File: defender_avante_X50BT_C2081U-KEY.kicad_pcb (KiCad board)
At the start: 2 copper layers, 172.7 x 61 mm, 85 parts, among them CN301 CONNECTOR_M_006_20_SPECIAL, J300 JUMPER, J301 JUMPER, J302 JUMPER, J303 JUMPER, J304 JUMPER, J305 JUMPER, J306 JUMPER, J307 JUMPER, J308 JUMPER, J309 JUMPER, J310 JUMPER, J311 JUMPER, J312 JUMPER, J313 JUMPER, J314 JUMPER, J315 JUMPER, J316 JUMPER, J317 JUMPER, J318 JUMPER, J319 JUMPER, J320 JUMPER, J321 JUMPER, J322 JUMPER, J323 JUMPER, J324 JUMPER, J325 JUMPER, J326 JUMPER, J327 JUMPER, J328 JUMPER, J329 JUMPER, J330 JUMPER, J331 JUMPER, J332 JUMPER, J333 JUMPER, J334 JUMPER, J335 JUMPER, J336 JUMPER, J337 JUMPER, Q300 BJT_NPN_GENERAL, U300 TM1668

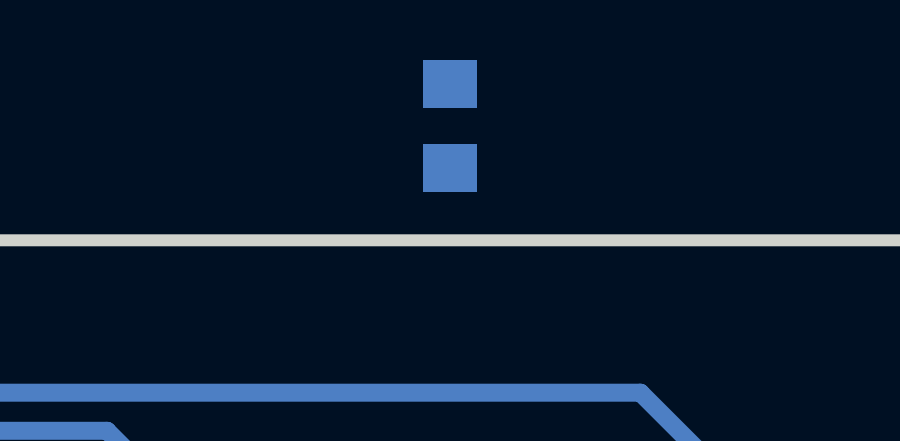
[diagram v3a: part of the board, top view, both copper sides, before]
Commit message: Удалена лишняя перемычка J314
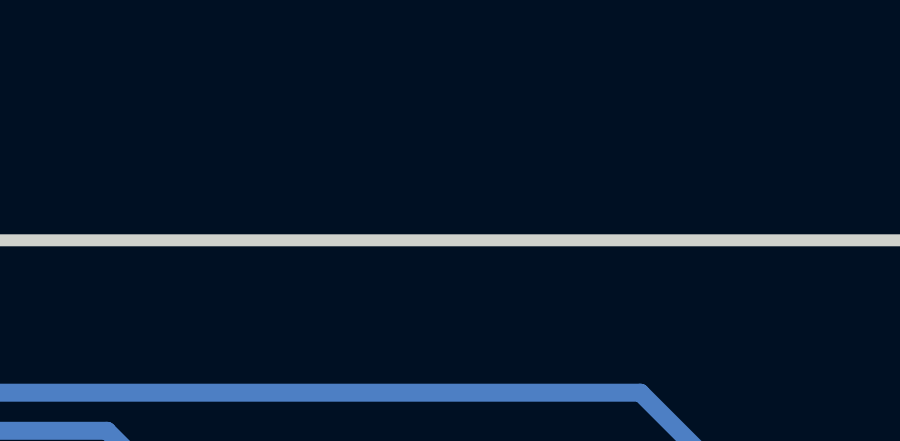
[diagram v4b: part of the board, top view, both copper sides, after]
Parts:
- removed the J314 at (118.1, 71.1)
- renumbered J315 to J314, J316 to J315, J317 to J316, J318 to J317, J319 to J318, J320 to J319, J321 to J320, J322 to J321, J323 to J322, J324 to J323, J325 to J324, J326 to J325, J327 to J326, J328 to J327, J329 to J328, J330 to J329, J331 to J330, J332 to J331, J333 to J332, J334 to J333, J335 to J334, J336 to J335, J337 to J336
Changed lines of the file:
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@@
     (tracks 502)
     (zones 0)
-    (modules 85)
+    (modules 84)
     (nets 49)
   )
@@
   (title_block
     (title defender_avante_X50BT_C2081U-KEY)
-    (date 2019-05-23)
+    (date 2019-06-04)
     (rev 2)
     (company "Igor Vladimirovich Ivanov")
@@
     (at 77.47 111.76 180)
     (attr smd)
-    (fp_text reference J332 (at 0 1.905 180) (layer B.SilkS)
+    (fp_text reference J331 (at 0 1.905 180) (layer B.SilkS)
       (effects (font (size 1 1) (thickness 0.2)) (justify mirror))
     )
@@
     (at 74.93 87.63 90)
     (attr smd)
-    (fp_text reference J334 (at 0 -1.905 270) (layer B.SilkS)
+    (fp_text reference J333 (at 0 -1.905 270) (layer B.SilkS)
       (effects (font (size 1 1) (thickness 0.2)) (justify mirror))
     )
@@
     (at 82.55 103.505 180)
     (attr smd)
-    (fp_text reference J329 (at 0 1.905 180) (layer B.SilkS)
+    (fp_text reference J328 (at 0 1.905 180) (layer B.SilkS)
       (effects (font (size 1 1) (thickness 0.2)) (justify mirror))
     )
@@
     (at 95.25 95.25 90)
     (attr smd)
-    (fp_text reference J322 (at 0 -1.905 270) (layer B.SilkS)
+    (fp_text reference J321 (at 0 -1.905 270) (layer B.SilkS)
       (effects (font (size 1 1) (thickness 0.2)) (justify mirror))
     )
@@
     (at 86.36 115.57 180)
     (attr smd)
-    (fp_text reference J326 (at 0 1.905 180) (layer B.SilkS)
+    (fp_text reference J325 (at 0 1.905 180) (layer B.SilkS)
       (effects (font (size 1 1) (thickness 0.2)) (justify mirror))
     )
@@
     (at 107.95 83.82 180)
     (attr smd)
-    (fp_text reference J315 (at 0 1.905 180) (layer B.SilkS)
+    (fp_text reference J314 (at 0 1.905 180) (layer B.SilkS)
       (effects (font (size 1 1) (thickness 0.2)) (justify mirror))
     )
@@
   )
   (module KCL:J-SMD-1206 (layer B.Cu)
-    (at 118.11 71.12 90)
-    (attr smd)
-    (fp_text reference J314 (at 0 -1.905 270) (layer B.SilkS)
-      (effects (font (size 1 1) (thickness 0.2)) (justify mirror))
-    )
-    (fp_text value JUMPER (at 1.905 4.445 180) (layer B.Fab) hide
-      (effects (font (size 1 1) (thickness 0.2)) (justify mirror))
-    )
-    (fp_line (start -1.6 0.8) (end -1.6 -0.8) (layer B.Fab) (width 0.2))
-    (fp_line (start -1.6 -0.8) (end 1.6 -0.8) (layer B.Fab) (width 0.2))
-    (fp_line (start 1.6 0.8) (end 1.6 -0.8) (layer B.Fab) (width 0.2))
-    (fp_line (start -1.6 0.8) (end 1.6 0.8) (layer B.Fab) (width 0.2))
-    (fp_line (start -2.413 1.016) (end -2.413 -1.016) (layer B.SilkS) (width 0.2))
-    (fp_line (start 2.413 1.016) (end 2.413 -1.016) (layer B.SilkS) (width 0.2))
-    (fp_line (start -2.413 1.016) (end 2.413 1.016) (layer B.SilkS) (width 0.2))
-    (fp_line (start -2.413 -1.016) (end 2.413 -1.016) (layer B.SilkS) (width 0.2))
-    (fp_line (start -0.381 0) (end 0.381 0) (layer B.SilkS) (width 0.2))
-    (fp_line (start -2.413 -1.016) (end -2.413 1.016) (layer B.CrtYd) (width 0.1))
-    (fp_line (start 2.413 -1.016) (end -2.413 -1.016) (layer B.CrtYd) (width 0.1))
-    (fp_line (start 2.413 1.016) (end 2.413 -1.016) (layer B.CrtYd) (width 0.1))
-    (fp_line (start -2.413 1.016) (end 2.413 1.016) (layer B.CrtYd) (width 0.1))
-    (pad J smd rect (at 1.4 0 90) (size 1.6 1.8) (layers B.Cu B.Mask)
-      (net 16 /B))
-    (pad J smd rect (at -1.4 0 90) (size 1.6 1.8) (layers B.Cu B.Mask)
-      (net 16 /B))
-  )
-  (module KCL:J-SMD-1206 (layer B.Cu)
     (at 156.21 106.68 90)
     (attr smd)
@@
     (at 69.85 101.6 90)
     (attr smd)
-    (fp_text reference J336 (at 0 1.905 270) (layer B.SilkS)
+    (fp_text reference J335 (at 0 1.905 270) (layer B.SilkS)
       (effects (font (size 1 1) (thickness 0.2)) (justify mirror))
     )
@@
     (at 97.79 115.57 180)
     (attr smd)
-    (fp_text reference J321 (at 4.445 0 180) (layer B.SilkS)
+    (fp_text reference J320 (at 4.445 0 180) (layer B.SilkS)
       (effects (font (size 1 1) (thickness 0.2)) (justify mirror))
     )
@@
     (at 100.33 87.63 90)
     (attr smd)
-    (fp_text reference J319 (at 0 -1.905 270) (layer B.SilkS)
+    (fp_text reference J318 (at 0 -1.905 270) (layer B.SilkS)
       (effects (font (size 1 1) (thickness 0.2)) (justify mirror))
     )
@@
   (module KCL:J-SMD-1206 (layer B.Cu)
     (at 107.95 103.505 180)
-    (fp_text reference J317 (at 0 1.905 180) (layer B.SilkS)
+    (fp_text reference J316 (at 0 1.905 180) (layer B.SilkS)
       (effects (font (size 1 1) (thickness 0.2)) (justify mirror))
     )
@@
     (at 87.63 87.63 90)
     (attr smd)
-    (fp_text reference J324 (at 0 -1.905 270) (layer B.SilkS)
+    (fp_text reference J323 (at 0 -1.905 270) (layer B.SilkS)
       (effects (font (size 1 1) (thickness 0.2)) (justify mirror))
     )
@@
     (at 86.36 111.76 180)
     (attr smd)
-    (fp_text reference J325 (at 0 1.905 180) (layer B.SilkS)
+    (fp_text reference J324 (at 0 1.905 180) (layer B.SilkS)
       (effects (font (size 1 1) (thickness 0.2)) (justify mirror))
     )
@@
     (at 105.41 113.03 180)
     (attr smd)
-    (fp_text reference J318 (at 0 1.905 180) (layer B.SilkS)
+    (fp_text reference J317 (at 0 1.905 180) (layer B.SilkS)
       (effects (font (size 1 1) (thickness 0.2)) (justify mirror))
     )
@@
     (at 69.85 96.52 90)
     (attr smd)
-    (fp_text reference J335 (at 0 1.905 270) (layer B.SilkS)
+    (fp_text reference J334 (at 0 1.905 270) (layer B.SilkS)
       (effects (font (size 1 1) (thickness 0.2)) (justify mirror))
     )
@@
     (at 67.31 96.52 90)
     (attr smd)
-    (fp_text reference J337 (at 0 -1.905 270) (layer B.SilkS)
+    (fp_text reference J336 (at 0 -1.905 270) (layer B.SilkS)
       (effects (font (size 1 1) (thickness 0.2)) (justify mirror))
     )
@@
     (at 107.95 87.63 90)
     (attr smd)
-    (fp_text reference J316 (at 0 -1.905 270) (layer B.SilkS)
+    (fp_text reference J315 (at 0 -1.905 270) (layer B.SilkS)
       (effects (font (size 1 1) (thickness 0.2)) (justify mirror))
     )
@@
     (at 77.47 115.57 180)
     (attr smd)
-    (fp_text reference J333 (at 0 1.905 180) (layer B.SilkS)
+    (fp_text reference J332 (at 0 1.905 180) (layer B.SilkS)
       (effects (font (size 1 1) (thickness 0.2)) (justify mirror))
     )
@@
     (at 82.55 83.82 180)
     (attr smd)
-    (fp_text reference J327 (at 0 1.905 180) (layer B.SilkS)
+    (fp_text reference J326 (at 0 1.905 180) (layer B.SilkS)
       (effects (font (size 1 1) (thickness 0.2)) (justify mirror))
     )
@@
     (at 77.47 95.25 180)
     (attr smd)
-    (fp_text reference J331 (at 0 1.905 180) (layer B.SilkS)
+    (fp_text reference J330 (at 0 1.905 180) (layer B.SilkS)
       (effects (font (size 1 1) (thickness 0.2)) (justify mirror))
     )
@@
     (at 91.44 111.76 180)
     (attr smd)
-    (fp_text reference J323 (at 0 1.905 180) (layer B.SilkS)
+    (fp_text reference J322 (at 0 1.905 180) (layer B.SilkS)
       (effects (font (size 1 1) (thickness 0.2)) (justify mirror))
     )
@@
     (at 97.79 113.03 180)
     (attr smd)
-    (fp_text reference J320 (at 0 1.905 180) (layer B.SilkS)
+    (fp_text reference J319 (at 0 1.905 180) (layer B.SilkS)
       (effects (font (size 1 1) (thickness 0.2)) (justify mirror))
     )
@@
     (at 81.28 111.76 90)
     (attr smd)
-    (fp_text reference J330 (at -4.445 0 270) (layer B.SilkS)
+    (fp_text reference J329 (at -4.445 0 270) (layer B.SilkS)
       (effects (font (size 1 1) (thickness 0.2)) (justify mirror))
     )
@@
     (at 82.55 87.63 90)
     (attr smd)
-    (fp_text reference J328 (at 0 -1.905 270) (layer B.SilkS)
-      (effects (font (size 1 1) (thickness 0.2)) (justify mirror))
-    )
+    (fp_text reference J327 (at 0 -1.905 270) (layer B.SilkS)
+      (effects (font (size 1 1) (thickness 0.2)) (justify mirror))
+    )

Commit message: Схема и плата оформлены корректно
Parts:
- added VLS300: VIRTUAL_LED-SPACER, KCL:VLS-BR, F.Cu at (229.9, 85.1)
- added VLS301: VIRTUAL_LED-SPACER, KCL:VLS-BR, F.Cu at (214.6, 105.4)
- W300: value ENCODER_CONTACTING_INC_B -> ENCODER_CONTACTING_INC_B_C
- moved R324 5.68 mm to (118.1, 85.1)
- moved R325 5.68 mm to (113.0, 87.6)
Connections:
- R324 pad 2: /A -> /B
- R325 pad 2: /B -> /A
- U300 pad 13: Net-(R325-Pad1) -> Net-(R324-Pad1)
- U300 pad 14: Net-(R324-Pad1) -> Net-(R325-Pad1)
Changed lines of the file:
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@@
   (general
     (thickness 1.5)
-    (drawings 27)
+    (drawings 21)
     (tracks 502)
     (zones 0)
-    (modules 84)
+    (modules 86)
     (nets 49)
   )
@@
     (add_net V)
   )
+  (module KCL:VLS-BR locked (layer F.Cu)
+    (at 214.63 105.41)
+    (attr virtual)
+    (fp_text reference VLS301 (at 0 7.62) (layer F.SilkS)
+      (effects (font (size 1 1) (thickness 0.2)))
+    )
+    (fp_text value VIRTUAL_LED-SPACER (at 28.575 1.27) (layer F.Fab) hide
+      (effects (font (size 1 1) (thickness 0.2)))
+    )
+    (fp_circle (center 0 0) (end 2.6 0) (layer F.CrtYd) (width 0.1))
+    (fp_circle (center 0 0) (end 2.6 0) (layer F.SilkS) (width 0.2))
+    (fp_circle (center 0 0) (end 2.6 0) (layer F.Fab) (width 0.2))
+  )
+  (module KCL:VLS-BR locked (layer F.Cu)
+    (at 229.87 85.09)
+    (attr virtual)
+    (fp_text reference VLS300 (at 0 -3.81) (layer F.SilkS)
+      (effects (font (size 1 1) (thickness 0.2)))
+    )
+    (fp_text value VIRTUAL_LED-SPACER (at 13.335 1.27) (layer F.Fab) hide
+      (effects (font (size 1 1) (thickness 0.2)))
+    )
+    (fp_circle (center 0 0) (end 2.6 0) (layer F.Fab) (width 0.2))
+    (fp_circle (center 0 0) (end 2.6 0) (layer F.SilkS) (width 0.2))
+    (fp_circle (center 0 0) (end 2.6 0) (layer F.CrtYd) (width 0.1))
+  )
   (module KCL:R-MFR-12 (layer F.Cu)
     (at 129.54 109.22)
@@
   )
   (module KCL:R-MFR-12 (layer F.Cu)
-    (at 113.03 87.63 180)
-    (fp_text reference R324 (at -6.35 0 180) (layer F.SilkS)
+    (at 118.11 85.09 180)
+    (fp_text reference R324 (at 0 2.54 180) (layer F.SilkS)
       (effects (font (size 1 1) (thickness 0.2)))
     )
-    (fp_text value RESISTOR_GENERAL (at -16.51 0 180) (layer F.Fab) hide
+    (fp_text value RESISTOR_GENERAL (at -11.43 0 180) (layer F.Fab) hide
       (effects (font (size 1 1) (thickness 0.2)))
     )
@@
     (fp_line (start 0.635 0.635) (end 1.27 0) (layer F.SilkS) (width 0.2))
     (pad 2 thru_hole rect (at 2.54 0 180) (size 2 2) (drill 0.5) (layers B.Cu B.Mask)
-      (net 17 /A))
+      (net 16 /B))
     (pad 1 thru_hole rect (at -2.54 0 180) (size 2 2) (drill 0.5) (layers B.Cu B.Mask)
       (net 42 "Net-(R324-Pad1)"))
   )
   (module KCL:R-MFR-12 (layer F.Cu)
-    (at 118.11 85.09 180)
-    (fp_text reference R325 (at 0 2.54 180) (layer F.SilkS)
+    (at 113.03 87.63 180)
+    (fp_text reference R325 (at -6.35 0 180) (layer F.SilkS)
       (effects (font (size 1 1) (thickness 0.2)))
     )
-    (fp_text value RESISTOR_GENERAL (at -11.43 0 180) (layer F.Fab) hide
+    (fp_text value RESISTOR_GENERAL (at -16.51 0 180) (layer F.Fab) hide
       (effects (font (size 1 1) (thickness 0.2)))
     )
@@
       (net 41 "Net-(R325-Pad1)"))
     (pad 2 thru_hole rect (at 2.54 0 180) (size 2 2) (drill 0.5) (layers B.Cu B.Mask)
-      (net 16 /B))
+      (net 17 /A))
   )
   (module KCL:R-MFR-12 (layer F.Cu)
@@
       (net 32 "Net-(U300-Pad15)"))
     (pad 14 smd rect (at 4.6 -5.715 180) (size 2.2 0.6) (layers B.Cu B.Mask)
-      (net 42 "Net-(R324-Pad1)"))
+      (net 41 "Net-(R325-Pad1)"))
     (pad 19 smd rect (at 4.6 0.635 180) (size 2.2 0.6) (layers B.Cu B.Mask)
       (net 31 "Net-(U300-Pad19)"))
@@
       (net 30 "Net-(U300-Pad16)"))
     (pad 13 smd rect (at 4.6 -6.985 180) (size 2.2 0.6) (layers B.Cu B.Mask)
-      (net 41 "Net-(R325-Pad1)"))
+      (net 42 "Net-(R324-Pad1)"))
     (pad 12 smd rect (at -4.6 -6.985 180) (size 2.2 0.6) (layers B.Cu B.Mask)
       (net 48 "Net-(R323-Pad2)"))
@@
   (module KCL:LED-ROUND-03.0-UNI-SH-SPACER locked (layer F.Cu)
     (at 229.87 85.09 45)
-    (fp_text reference LED300 (at 4.041115 -4.041115 180) (layer F.SilkS)
+    (fp_text reference LED300 (at 5.388154 -5.388154 180) (layer F.SilkS)
       (effects (font (size 1 1) (thickness 0.2)))
     )
@@
       (effects (font (size 1 1) (thickness 0.2)))
     )
-    (fp_text value ENCODER_CONTACTING_INC_B (at 0 -23.495) (layer F.Fab) hide
+    (fp_text value ENCODER_CONTACTING_INC_B_C (at 0 -24.13) (layer F.Fab) hide
       (effects (font (size 1 1) (thickness 0.2)))
     )
@@
     (effects (font (size 1 1) (thickness 0.2)))
   )
-  (gr_text BLUE (at 229.87 81.28) (layer F.SilkS)
+  (gr_text BLUE (at 229.87 79.375) (layer F.SilkS)
     (effects (font (size 1 1) (thickness 0.2)))
   )
@@
     (effects (font (size 1 1) (thickness 0.2)))
   )
-  (gr_circle (center 229.87 85.09) (end 232.47 85.09) (layer F.SilkS) (width 0.2))
-  (gr_circle (center 229.87 85.09) (end 232.47 85.09) (layer F.Fab) (width 0.2))
-  (gr_circle (center 229.87 85.09) (end 232.47 85.09) (layer F.CrtYd) (width 0.1))
-  (gr_circle (center 214.63 105.41) (end 217.23 105.41) (layer F.SilkS) (width 0.2))
-  (gr_circle (center 214.63 105.41) (end 217.23 105.41) (layer F.Fab) (width 0.2))
-  (gr_circle (center 214.63 105.41) (end 217.23 105.41) (layer F.CrtYd) (width 0.1))
   (gr_line (start 234.315 74.93) (end 234.315 135.89) (layer Edge.Cuts) (width 0.4))
   (gr_line (start 179.07 135.89) (end 234.315 135.89) (layer Edge.Cuts) (width 0.4))
@@
   (segment (start 214.63 77.47) (end 189.33 77.47) (width 0.6) (layer B.Cu) (net 40))
   (segment (start 189.33 77.47) (end 185.52 81.28) (width 0.6) (layer B.Cu) (net 40))
-  (segment (start 132.08 89.535) (end 127.635 85.09) (width 0.6) (layer B.Cu) (net 41))
-  (segment (start 132.08 101.6) (end 132.08 89.535) (width 0.6) (layer B.Cu) (net 41))
-  (segment (start 124.94 106.68) (end 127 106.68) (width 0.6) (layer B.Cu) (net 41))
-  (segment (start 127 106.68) (end 132.08 101.6) (width 0.6) (layer B.Cu) (net 41))
-  (segment (start 120.65 85.09) (end 127.635 85.09) (width 0.6) (layer B.Cu) (net 41))
-  (segment (start 126.365 105.41) (end 130.81 100.965) (width 0.6) (layer B.Cu) (net 42))
-  (segment (start 126.365 105.41) (end 124.94 105.41) (width 0.6) (layer B.Cu) (net 42))
-  (segment (start 130.81 90.17) (end 130.81 100.965) (width 0.6) (layer B.Cu) (net 42))
-  (segment (start 128.27 87.63) (end 130.81 90.17) (width 0.6) (layer B.Cu) (net 42))
-  (segment (start 128.27 87.63) (end 115.57 87.63) (width 0.6) (layer B.Cu) (net 42))
+  (segment (start 132.08 89.535) (end 127.635 85.09) (width 0.6) (layer B.Cu) (net 42))
+  (segment (start 132.08 101.6) (end 132.08 89.535) (width 0.6) (layer B.Cu) (net 42))
+  (segment (start 124.94 106.68) (end 127 106.68) (width 0.6) (layer B.Cu) (net 42))
+  (segment (start 127 106.68) (end 132.08 101.6) (width 0.6) (layer B.Cu) (net 42))
+  (segment (start 120.65 85.09) (end 127.635 85.09) (width 0.6) (layer B.Cu) (net 42))
+  (segment (start 126.365 105.41) (end 130.81 100.965) (width 0.6) (layer B.Cu) (net 41))
+  (segment (start 126.365 105.41) (end 124.94 105.41) (width 0.6) (layer B.Cu) (net 41))
+  (segment (start 130.81 90.17) (end 130.81 100.965) (width 0.6) (layer B.Cu) (net 41))
+  (segment (start 128.27 87.63) (end 130.81 90.17) (width 0.6) (layer B.Cu) (net 41))
+  (segment (start 128.27 87.63) (end 115.57 87.63) (width 0.6) (layer B.Cu) (net 41))
   (segment (start 132.08 111.76) (end 134.62 111.76) (width 0.6) (layer B.Cu) (net 43))
   (segment (start 134.14 105.41) (end 135.89 105.41) (width 0.6) (layer B.Cu) (net 43))
